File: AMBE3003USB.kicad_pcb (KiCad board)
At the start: 2 copper layers, 95 x 85 mm, 84 parts, among them J1 McBSP, J2 USB_OTG, J4 CODEC, P1 GND, P2 Config, P3 3v3, P4 VSET, P5 HARD RESET, P6 SEQ, P7 3v3, P8 ACONF, P9 GND, Q1 BC847, U1 AMBE3003, U2 TPS75005RGW, U3 FT232RL, X1 29.4912

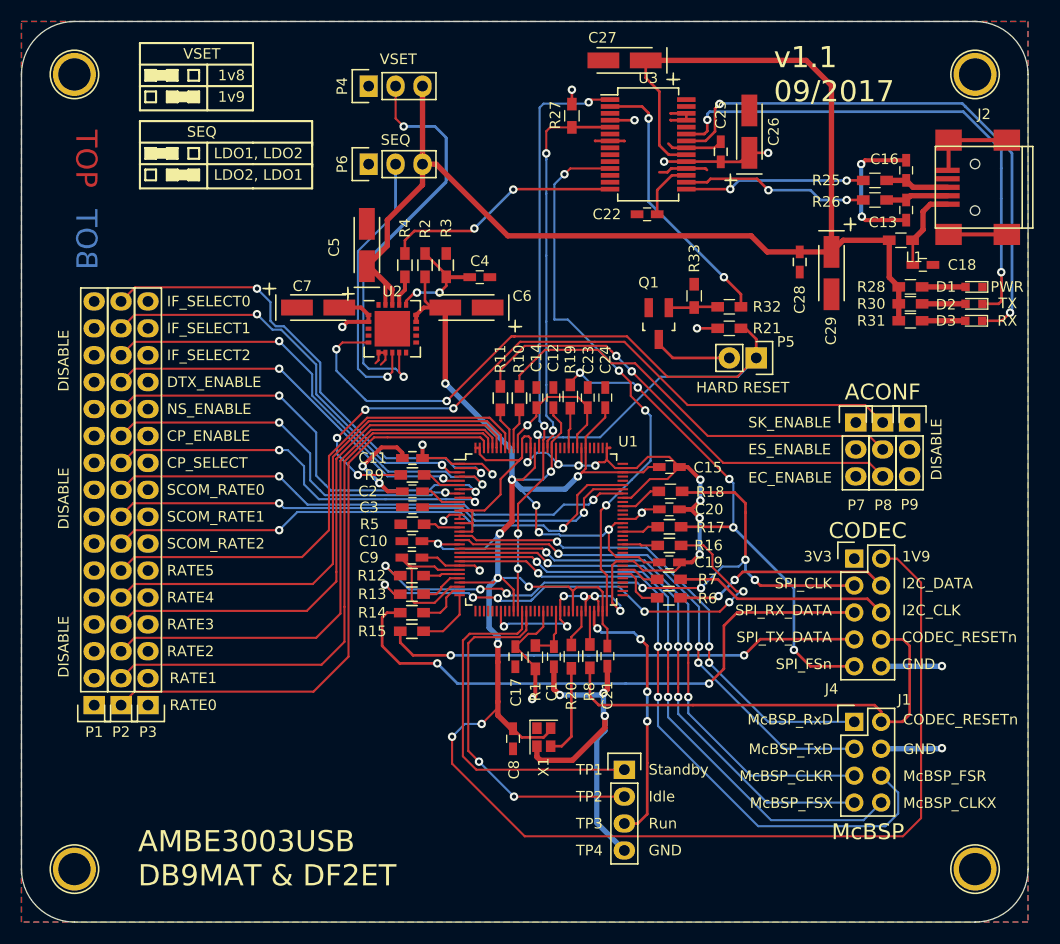
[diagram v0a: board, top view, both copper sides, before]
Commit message: Make BCu GND and add thermal pad for TPS75005
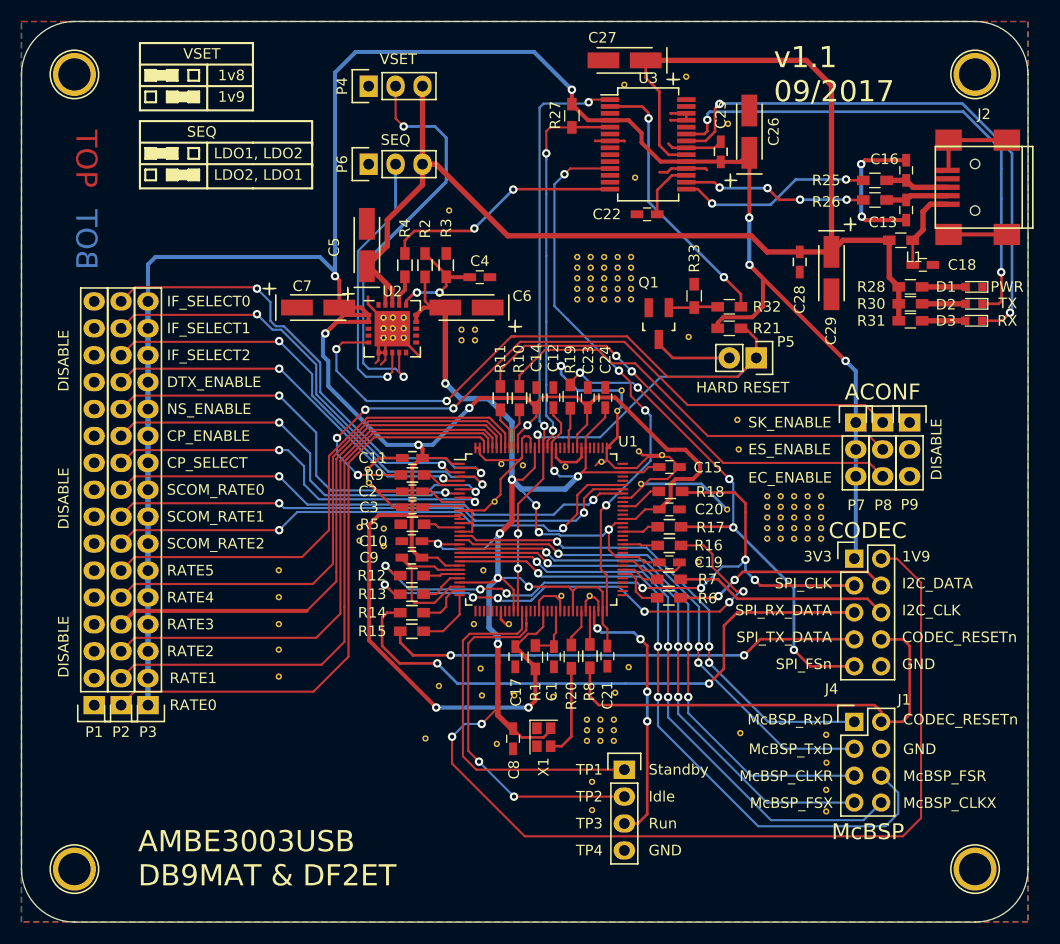
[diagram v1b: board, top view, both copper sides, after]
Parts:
- added REF**11: VIA-0.6mm, VIA:VIA-0.6mm, F.Cu at (95.0, 77.8)
- added REF**11: VIA-0.6mm, VIA:VIA-0.6mm, F.Cu at (56.3, 99.8)
- added REF**11: VIA-0.6mm, VIA:VIA-0.6mm, F.Cu at (99.6, 85.6)
- added REF**11: VIA-0.6mm, VIA:VIA-0.6mm, F.Cu at (99.7, 88.4)
- added REF**11: VIA-0.6mm, VIA:VIA-0.6mm, F.Cu at (85.9, 122.4)
- added REF**11: VIA-0.6mm, VIA:VIA-0.6mm, F.Cu at (85.9, 119.8)
- added REF**11: VIA-0.6mm, VIA:VIA-0.6mm, F.Cu at (108.0, 122.6)
- added REF**11: VIA-0.6mm, VIA:VIA-0.6mm, F.Cu at (108.0, 118.0)
- added REF**11: VIA-0.6mm, VIA:VIA-0.6mm, F.Cu at (108.0, 115.3)
- added REF**11: VIA-0.6mm, VIA:VIA-0.6mm, F.Cu at (108.0, 120.5)
- added REF**11: VIA-0.6mm, VIA:VIA-0.6mm, F.Cu at (99.8, 115.2)
- added REF**11: VIA-0.6mm, VIA:VIA-0.6mm, F.Cu at (75.6, 99.8)
- added REF**11: VIA-0.6mm, VIA:VIA-0.6mm, F.Cu at (88.0, 111.4)
- added REF**11: VIA-0.6mm, VIA:VIA-0.6mm, F.Cu at (89.3, 108.9)
- added REF**11: VIA-0.6mm, VIA:VIA-0.6mm, F.Cu at (74.7, 104.9)
- added REF**11: VIA-0.6mm, VIA:VIA-0.6mm, F.Cu at (75.5, 111.6)
- added REF**11: VIA-0.6mm, VIA:VIA-0.6mm, F.Cu at (75.3, 109.1)
- added REF**11: VIA-0.6mm, VIA:VIA-0.6mm, F.Cu at (90.5, 91.6)
- added REF**11: VIA-0.6mm, VIA:VIA-0.6mm, F.Cu at (95.9, 99.0)
- added REF**11: VIA-0.6mm, VIA:VIA-0.6mm, F.Cu at (88.2, 84.8)
- added REF**11: VIA-0.6mm, VIA:VIA-0.6mm, F.Cu at (64.8, 91.5)
- added REF**11: VIA-0.6mm, VIA:VIA-0.6mm, F.Cu at (64.7, 90.3)
- added REF**11: VIA-0.6mm, VIA:VIA-0.6mm, F.Cu at (77.3, 89.8)
- added REF**11: VIA-0.6mm, VIA:VIA-0.6mm, F.Cu at (66.2, 97.5)
- added REF**11: VIA-0.6mm, VIA:VIA-0.6mm, F.Cu at (66.2, 95.9)
- added REF**11: VIA-0.6mm, VIA:VIA-0.6mm, F.Cu at (63.9, 97.0)
- added REF**11: VIA-0.6mm, VIA:VIA-0.6mm, F.Cu at (63.9, 95.7)
- added REF**11: VIA-0.6mm, VIA:VIA-0.6mm, F.Cu at (70.1, 115.7)
- added REF**11: VIA-0.6mm, VIA:VIA-0.6mm, F.Cu at (71.4, 110.7)
- added REF**11: VIA-0.6mm, VIA:VIA-0.6mm, F.Cu at (78.0, 104.9)
- added REF**11: VIA-0.6mm, VIA:VIA-0.6mm, F.Cu at (83.0, 102.2)
- added REF**11: VIA-0.6mm, VIA:VIA-0.6mm, F.Cu at (85.6, 102.2)
- added REF**11: VIA-0.6mm, VIA:VIA-0.6mm, F.Cu at (82.2, 111.7)
- added REF**11: VIA-0.6mm, VIA:VIA-0.6mm, F.Cu at (76.7, 93.3)
- added REF**11: VIA-0.6mm, VIA:VIA-0.6mm, F.Cu at (76.9, 116.2)
- added REF**11: VIA-0.6mm, VIA:VIA-0.6mm, F.Cu at (78.5, 111.6)
- added REF**11: VIA-0.6mm, VIA:VIA-0.6mm, F.Cu at (88.6, 82.8)
- added REF**11: VIA-0.6mm, VIA:VIA-0.6mm, F.Cu at (86.7, 89.6)
- added REF**11: VIA-0.6mm, VIA:VIA-0.6mm, F.Cu at (68.1, 77.9)
- added REF**11: VIA-0.6mm, VIA:VIA-0.6mm, F.Cu at (68.1, 77.0)
- added REF**11: VIA-0.6mm, VIA:VIA-0.6mm, F.Cu at (67.1, 77.0)
- added REF**11: VIA-0.6mm, VIA:VIA-0.6mm, F.Cu at (67.1, 77.9)
- added REF**11: VIA-0.6mm, VIA:VIA-0.6mm, F.Cu at (66.2, 77.9)
- added REF**11: VIA-0.6mm, VIA:VIA-0.6mm, F.Cu at (66.2, 77.0)
- added REF**11: VIA-0.6mm, VIA:VIA-0.6mm, F.Cu at (72.4, 65.8)
- added REF**11: VIA-0.6mm, VIA:VIA-0.6mm, F.Cu at (68.1, 75.9)
- added REF**11: VIA-0.6mm, VIA:VIA-0.6mm, F.Cu at (67.1, 75.9)
- added REF**11: VIA-0.6mm, VIA:VIA-0.6mm, F.Cu at (66.2, 75.9)
- added REF**11: VIA-0.6mm, VIA:VIA-0.6mm, F.Cu at (79.3, 89.9)
- added REF**11: VIA-0.6mm, VIA:VIA-0.6mm, F.Cu at (83.3, 90.0)
- added REF**11: VIA-0.6mm, VIA:VIA-0.6mm, F.Cu at (92.5, 88.9)
- added REF**11: VIA-0.6mm, VIA:VIA-0.6mm, F.Cu at (90.3, 88.6)
- added REF**11: VIA-0.6mm, VIA:VIA-0.6mm, F.Cu at (98.6, 94.1)
- added REF**11: VIA-0.6mm, VIA:VIA-0.6mm, F.Cu at (56.3, 109.8)
- added REF**11: VIA-0.6mm, VIA:VIA-0.6mm, F.Cu at (56.3, 107.3)
- added REF**11: VIA-0.6mm, VIA:VIA-0.6mm, F.Cu at (56.3, 104.9)
- added REF**11: VIA-0.6mm, VIA:VIA-0.6mm, F.Cu at (56.3, 102.3)
- added REF**111: VIA-0.6mm, VIA:VIA-0.6mm, F.Cu at (73.5, 77.1)
- added REF**111: VIA-0.6mm, VIA:VIA-0.6mm, F.Cu at (85.4, 113.9)
- added REF**1111: VIA-0.6mm, VIA:VIA-0.6mm, F.Cu at (102.4, 92.8)
- added REF**1112: VIA-0.6mm, VIA:VIA-0.6mm, F.Cu at (102.4, 93.8)
- added REF**1113: VIA-0.6mm, VIA:VIA-0.6mm, F.Cu at (102.4, 94.8)
- added REF**1114: VIA-0.6mm, VIA:VIA-0.6mm, F.Cu at (102.4, 95.8)
- added REF**1115: VIA-0.6mm, VIA:VIA-0.6mm, F.Cu at (102.4, 96.8)
- added REF**112: VIA-0.6mm, VIA:VIA-0.6mm, F.Cu at (73.5, 78.1)
- added REF**112: VIA-0.6mm, VIA:VIA-0.6mm, F.Cu at (85.4, 114.9)
- added REF**1121: VIA-0.6mm, VIA:VIA-0.6mm, F.Cu at (103.7, 92.8)
- added REF**1122: VIA-0.6mm, VIA:VIA-0.6mm, F.Cu at (103.7, 93.8)
- added REF**1123: VIA-0.6mm, VIA:VIA-0.6mm, F.Cu at (103.7, 94.8)
- added REF**1124: VIA-0.6mm, VIA:VIA-0.6mm, F.Cu at (103.7, 95.8)
- added REF**1125: VIA-0.6mm, VIA:VIA-0.6mm, F.Cu at (103.7, 96.8)
- added REF**113: VIA-0.6mm, VIA:VIA-0.6mm, F.Cu at (85.4, 115.9)
- added REF**1131: VIA-0.6mm, VIA:VIA-0.6mm, F.Cu at (104.9, 92.8)
- added REF**1132: VIA-0.6mm, VIA:VIA-0.6mm, F.Cu at (104.9, 93.8)
- added REF**1133: VIA-0.6mm, VIA:VIA-0.6mm, F.Cu at (104.9, 94.8)
- added REF**1134: VIA-0.6mm, VIA:VIA-0.6mm, F.Cu at (104.9, 95.8)
- added REF**1135: VIA-0.6mm, VIA:VIA-0.6mm, F.Cu at (104.9, 96.8)
- added REF**1141: VIA-0.6mm, VIA:VIA-0.6mm, F.Cu at (106.2, 92.8)
- added REF**1142: VIA-0.6mm, VIA:VIA-0.6mm, F.Cu at (106.2, 93.8)
- added REF**1143: VIA-0.6mm, VIA:VIA-0.6mm, F.Cu at (106.2, 94.8)
- added REF**1144: VIA-0.6mm, VIA:VIA-0.6mm, F.Cu at (106.2, 95.8)
- added REF**1145: VIA-0.6mm, VIA:VIA-0.6mm, F.Cu at (106.2, 96.8)
- added REF**1151: VIA-0.6mm, VIA:VIA-0.6mm, F.Cu at (107.5, 92.8)
- added REF**1152: VIA-0.6mm, VIA:VIA-0.6mm, F.Cu at (107.5, 93.8)
- added REF**1153: VIA-0.6mm, VIA:VIA-0.6mm, F.Cu at (107.5, 94.8)
- added REF**1154: VIA-0.6mm, VIA:VIA-0.6mm, F.Cu at (107.5, 95.8)
- added REF**1155: VIA-0.6mm, VIA:VIA-0.6mm, F.Cu at (107.5, 96.8)
- added REF**121: VIA-0.6mm, VIA:VIA-0.6mm, F.Cu at (74.8, 77.1)
- added REF**121: VIA-0.6mm, VIA:VIA-0.6mm, F.Cu at (86.6, 113.9)
- added REF**1211: VIA-0.6mm, VIA:VIA-0.6mm, F.Cu at (84.5, 70.2)
- added REF**1212: VIA-0.6mm, VIA:VIA-0.6mm, F.Cu at (84.5, 71.2)
- added REF**1213: VIA-0.6mm, VIA:VIA-0.6mm, F.Cu at (84.5, 72.2)
- added REF**1214: VIA-0.6mm, VIA:VIA-0.6mm, F.Cu at (84.5, 73.2)
- added REF**1215: VIA-0.6mm, VIA:VIA-0.6mm, F.Cu at (84.5, 74.2)
- added REF**122: VIA-0.6mm, VIA:VIA-0.6mm, F.Cu at (74.8, 78.1)
- added REF**122: VIA-0.6mm, VIA:VIA-0.6mm, F.Cu at (86.6, 114.9)
- added REF**1221: VIA-0.6mm, VIA:VIA-0.6mm, F.Cu at (85.7, 70.2)
- added REF**1222: VIA-0.6mm, VIA:VIA-0.6mm, F.Cu at (85.7, 71.2)
- added REF**1223: VIA-0.6mm, VIA:VIA-0.6mm, F.Cu at (85.7, 72.2)
- added REF**1224: VIA-0.6mm, VIA:VIA-0.6mm, F.Cu at (85.7, 73.2)
- added REF**1225: VIA-0.6mm, VIA:VIA-0.6mm, F.Cu at (85.7, 74.2)
- added REF**123: VIA-0.6mm, VIA:VIA-0.6mm, F.Cu at (86.6, 115.9)
- added REF**1231: VIA-0.6mm, VIA:VIA-0.6mm, F.Cu at (87.0, 70.2)
- added REF**1232: VIA-0.6mm, VIA:VIA-0.6mm, F.Cu at (87.0, 71.2)
- added REF**1233: VIA-0.6mm, VIA:VIA-0.6mm, F.Cu at (87.0, 72.2)
- added REF**1234: VIA-0.6mm, VIA:VIA-0.6mm, F.Cu at (87.0, 73.2)
- added REF**1235: VIA-0.6mm, VIA:VIA-0.6mm, F.Cu at (87.0, 74.2)
- added REF**1241: VIA-0.6mm, VIA:VIA-0.6mm, F.Cu at (88.3, 70.2)
- added REF**1242: VIA-0.6mm, VIA:VIA-0.6mm, F.Cu at (88.3, 71.2)
- added REF**1243: VIA-0.6mm, VIA:VIA-0.6mm, F.Cu at (88.3, 72.2)
- added REF**1244: VIA-0.6mm, VIA:VIA-0.6mm, F.Cu at (88.3, 73.2)
- added REF**1245: VIA-0.6mm, VIA:VIA-0.6mm, F.Cu at (88.3, 74.2)
- added REF**1251: VIA-0.6mm, VIA:VIA-0.6mm, F.Cu at (88.9, 54.0)
- added REF**1251: VIA-0.6mm, VIA:VIA-0.6mm, F.Cu at (94.7, 53.2)
- added REF**1251: VIA-0.6mm, VIA:VIA-0.6mm, F.Cu at (89.9, 62.7)
- added REF**1251: VIA-0.6mm, VIA:VIA-0.6mm, F.Cu at (98.7, 57.7)
- added REF**1251: VIA-0.6mm, VIA:VIA-0.6mm, F.Cu at (89.5, 70.2)
- added REF**1252: VIA-0.6mm, VIA:VIA-0.6mm, F.Cu at (89.5, 71.2)
- added REF**1253: VIA-0.6mm, VIA:VIA-0.6mm, F.Cu at (89.5, 72.2)
- added REF**1254: VIA-0.6mm, VIA:VIA-0.6mm, F.Cu at (89.5, 73.2)
- added REF**1255: VIA-0.6mm, VIA:VIA-0.6mm, F.Cu at (89.5, 74.2)
- added REF**131: VIA-0.6mm, VIA:VIA-0.6mm, F.Cu at (87.9, 113.9)
- added REF**132: VIA-0.6mm, VIA:VIA-0.6mm, F.Cu at (87.9, 114.9)
- added REF**133: VIA-0.6mm, VIA:VIA-0.6mm, F.Cu at (87.9, 115.9)
- U2: value TPS75005RGW -> TPS75005RGW_wPin21
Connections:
- U1 pad 48: (no net) -> GND
- U2 pad 21: (no net) -> GND
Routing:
- net +3V3: track 67.8 -> 332.1 mm, vias 13 -> 11
- net GND: track 222.1 -> 170.7 mm, vias 23 -> 3
- net Net-(R25-Pad1): track 17.0 -> 18.3 mm
- net UART_RTS: track 52.9 -> 52.2 mm
- net Net-(R26-Pad1): track 17.7 -> 17.4 mm, vias 2 -> 4
- added copper zone on B.Cu, net GND
- removed copper zone on B.Cu, net +3V3

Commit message: Make PARTIY available on jumper header
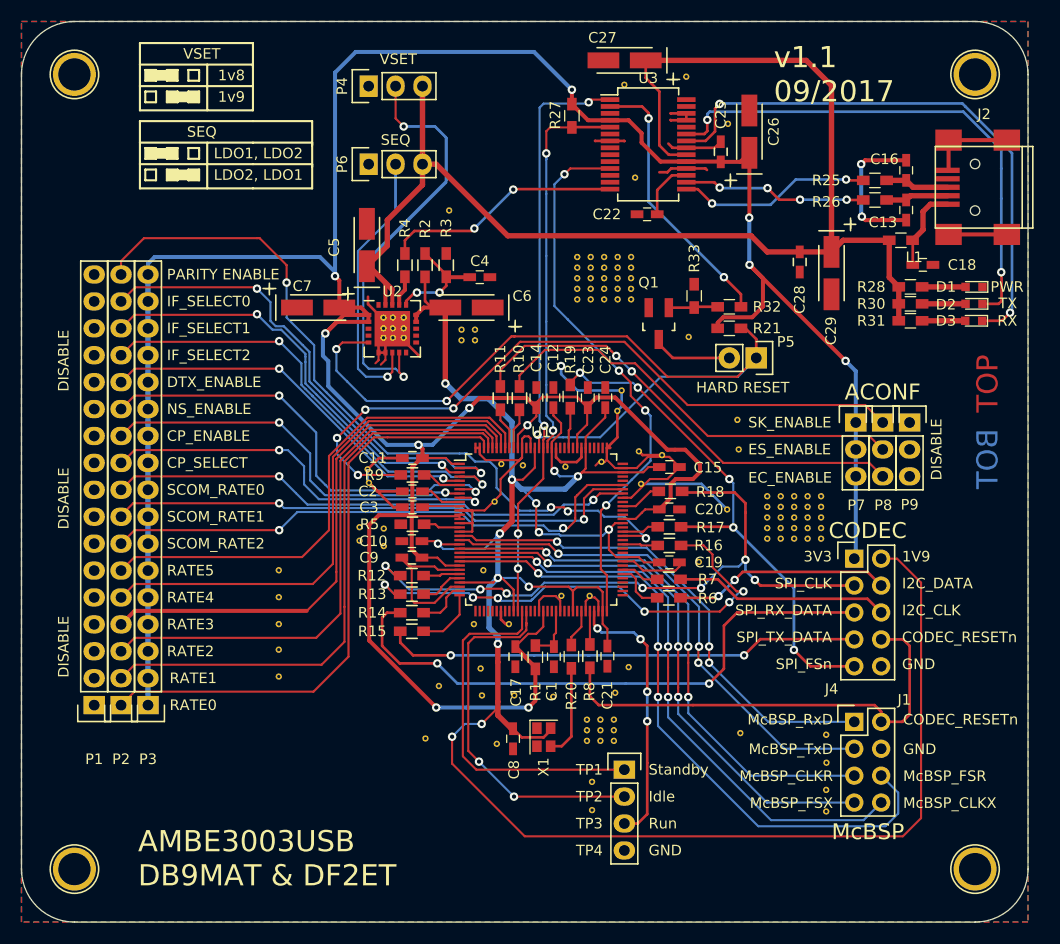
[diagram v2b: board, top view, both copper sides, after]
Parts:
- P1, P2, P3: footprint Pin_Headers:Pin_Header_Straight_1x16 -> Pin_Headers:Pin_Header_Straight_1x17
- U1: footprint Housings_QFP:LQFP-128_14x14mm_Pitch0.4mm -> Housings_QFP:TQFP-128_14x14mm_Pitch0.4mm
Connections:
- U1 pad 79: (no net) -> PARITY_ENABLE
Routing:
- net PARITY_ENABLE: track 0.00 -> 71.9 mm, vias 0 -> 4
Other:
- board text added: "PARITY ENABLE"
